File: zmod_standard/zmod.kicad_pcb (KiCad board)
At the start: 6 copper layers, 50 x 70 mm, 13 parts, among them J2 QTH-020-01-X-D-DP-A

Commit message: zmod_standard work
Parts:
- removed J2: QTH-020-01-X-D-DP-A, QTH:SAMTEC_QTH-020-01-X-D-DP-A
- removed R3: 100, Resistor_SMD:R_0603_1608Metric
- added J1: QTE-020-01-X-D-A, QTE:SAMTEC_QTE-020-01-X-D-A, F.Cu at (125.0, 57.0)
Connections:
- R1 pad 2: Net-(J2-Pad14) -> /led0
- R2 pad 2: Net-(J2-Pad16) -> /led1
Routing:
- net /hss1_N: track 353.6 -> 0.00 mm, vias 12 -> 0
- net /hss1_P: track 353.5 -> 0.00 mm, vias 12 -> 0
- net Net-(J2-Pad14): track 52.9 -> 0.00 mm, vias 2 -> 0
- net Net-(J2-Pad16): track 52.8 -> 0.00 mm, vias 2 -> 0
- net /led0: track 0.00 -> 49.9 mm
- net /led1: track 0.00 -> 49.7 mm, vias 0 -> 2
- net /lvdsclk_P: track 27.2 -> 0.00 mm
- net /lvdsclk_N: track 24.2 -> 0.00 mm
- net /lvds1_P: track 15.5 -> 0.00 mm, vias 2 -> 0
- net /lvds1_N: track 12.8 -> 0.00 mm, vias 2 -> 0
- net /lvds0_P: track 12.1 -> 0.00 mm, vias 2 -> 0
- net /d4_P: track 0.00 -> 11.8 mm, vias 0 -> 2
- net /d0_N: track 0.00 -> 11.3 mm, vias 0 -> 2
- net /d1_N: track 0.00 -> 11.3 mm, vias 0 -> 2
- net /lvds0_N: track 10.8 -> 0.00 mm, vias 2 -> 0
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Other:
- board text added: "ZMOD Standard Rev 1.0 WWW.HDLGUY.COM"
- board text removed: "ZMOD TXR-2 Rev 1.0 WWW.HDLGUY.COM"

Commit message: removed redundant fill planes on zmod boards
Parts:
- moved H2 5.00 mm to (140.0, 115.0)
- moved H5 5.00 mm to (139.5, 57.0)
- moved H6 5.00 mm to (140.0, 67.0)
- moved J1 2.50 mm to (122.5, 57.0)
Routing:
- net /led0: track 49.9 -> 0.00 mm
- net /led1: track 49.7 -> 0.00 mm, vias 2 -> 0
- net GND: track 14.9 -> 0.00 mm, vias 10 -> 0
- net /d4_P: track 11.8 -> 0.00 mm, vias 2 -> 0
- net /d0_N: track 11.3 -> 0.00 mm, vias 2 -> 0
- net /d1_N: track 11.3 -> 0.00 mm, vias 2 -> 0
- net /d4_N: track 10.7 -> 0.00 mm, vias 2 -> 0
- net /d0_P: track 10.4 -> 0.00 mm, vias 2 -> 0
- net /d1_P: track 9.39 -> 0.00 mm, vias 2 -> 0
- net /d5_P: track 9.13 -> 0.00 mm, vias 2 -> 0
- net /R_GA: track 8.76 -> 0.00 mm
- net /d5_N: track 8.40 -> 0.00 mm, vias 2 -> 0
- net /p2c_clk_N: track 7.01 -> 0.00 mm
- net /p2c_clk_P: track 7.01 -> 0.00 mm
- net /s24: track 4.44 -> 0.00 mm
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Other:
- board size 50 x 70 mm -> 45 x 70 mm

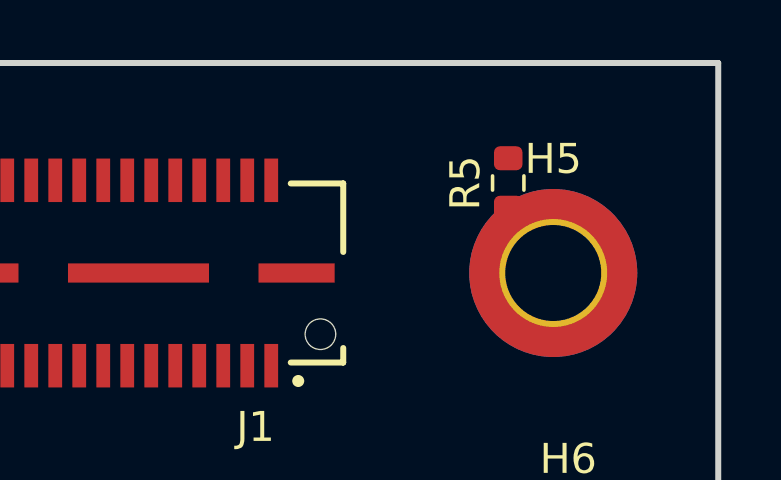
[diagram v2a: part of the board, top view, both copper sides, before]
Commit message: organizing local libraries, footprint and symbol
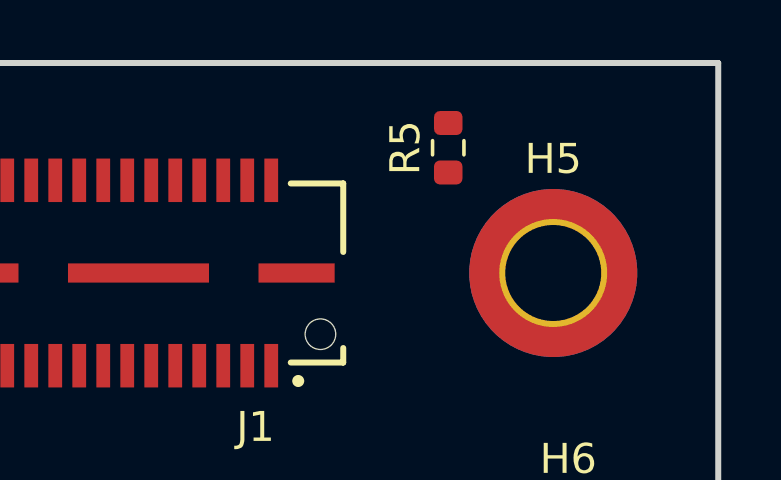
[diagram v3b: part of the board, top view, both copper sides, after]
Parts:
- J1: footprint QTE:SAMTEC_QTE-020-01-X-D-A -> pedrolib:SAMTEC_QTE-020-01-X-D-A
- moved R5 2.32 mm to (136.0, 52.8)
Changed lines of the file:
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@@
     (descr "LED SMD 0603 (1608 Metric), square (rectangular) end terminal, IPC_7351 nominal, (Body size source: http://www.tortai-tech.com/upload/download/2011102023233369053.pdf), generated with kicad-footprint-generator")
     (tags "LED")
-    (property "Sheetfile" "zmod.kicad_sch")
+    (property "Sheetfile" "File: zmod.kicad_sch")
     (property "Sheetname" "")
     (attr smd)
@@
     (descr "LED SMD 0603 (1608 Metric), square (rectangular) end terminal, IPC_7351 nominal, (Body size source: http://www.tortai-tech.com/upload/download/2011102023233369053.pdf), generated with kicad-footprint-generator")
     (tags "LED")
-    (property "Sheetfile" "zmod.kicad_sch")
+    (property "Sheetfile" "File: zmod.kicad_sch")
     (property "Sheetname" "")
     (attr smd)
@@
     (descr "Mounting Hole 3.2mm, M3, DIN965")
     (tags "mounting hole 3.2mm m3 din965")
-    (property "Sheetfile" "zmod.kicad_sch")
+    (property "Sheetfile" "File: zmod.kicad_sch")
     (property "Sheetname" "")
     (attr exclude_from_pos_files)
@@
     (descr "Resistor SMD 0603 (1608 Metric), square (rectangular) end terminal, IPC_7351 nominal, (Body size source: IPC-SM-782 page 72, https://www.pcb-3d.com/wordpress/wp-content/uploads/ipc-sm-782a_amendment_1_and_2.pdf), generated with kicad-footprint-generator")
     (tags "resistor")
-    (property "Sheetfile" "zmod.kicad_sch")
+    (property "Sheetfile" "File: zmod.kicad_sch")
     (property "Sheetname" "")
     (attr smd)
@@
     (descr "Mounting Hole 3.2mm, M3, DIN965")
     (tags "mounting hole 3.2mm m3 din965")
-    (property "Sheetfile" "zmod.kicad_sch")
+    (property "Sheetfile" "File: zmod.kicad_sch")
     (property "Sheetname" "")
     (attr exclude_from_pos_files)
@@
     (descr "Mounting Hole 3.2mm, M3, DIN965")
     (tags "mounting hole 3.2mm m3 din965")
-    (property "Sheetfile" "zmod.kicad_sch")
+    (property "Sheetfile" "File: zmod.kicad_sch")
     (property "Sheetname" "")
     (attr exclude_from_pos_files)
@@
     (descr "Mounting Hole 3.2mm, M3, DIN965")
     (tags "mounting hole 3.2mm m3 din965")
-    (property "Sheetfile" "zmod.kicad_sch")
+    (property "Sheetfile" "File: zmod.kicad_sch")
     (property "Sheetname" "")
     (attr exclude_from_pos_files)
@@
     (descr "Mounting Hole 3.2mm, M3, DIN965")
     (tags "mounting hole 3.2mm m3 din965")
-    (property "Sheetfile" "zmod.kicad_sch")
+    (property "Sheetfile" "File: zmod.kicad_sch")
     (property "Sheetname" "")
     (attr exclude_from_pos_files)
@@
       (net 9 "unconnected-(H4-Pad1)") (pinfunction "1") (pintype "input"))
   )
-  (footprint "QTE:SAMTEC_QTE-020-01-X-D-A" locked (layer "F.Cu")
+  (footprint "pedrolib:SAMTEC_QTE-020-01-X-D-A" locked (layer "F.Cu")
     (at 122.5 57 180)
     (property "MANUFACTURER" "Samtec")
@@
     (property "PARTREV" "K")
     (property "STANDARD" "Manufacturer Recommendations")
-    (property "Sheetfile" "zmod.kicad_sch")
+    (property "Sheetfile" "File: zmod.kicad_sch")
     (property "Sheetname" "")
     (attr through_hole)
@@
       (effects (font (size 1 1) (thickness 0.15)))
     )
-    (fp_line (start -8.25 -2.9845) (end -10 -2.9845) (layer "F.SilkS") (width 0.2))
-    (fp_line (start 8.25 -2.9845) (end 10 -2.9845) (layer "F.SilkS") (width 0.2))
-    (fp_line (start 10 -2.9845) (end 10 -2.5) (layer "F.SilkS") (width 0.2))
-    (fp_line (start -10 0.7) (end -10 2.9845) (layer "F.SilkS") (width 0.2))
     (fp_line (start 8.25 2.9845) (end 10 2.9845) (layer "F.SilkS") (width 0.2))
     (fp_line (start -10 2.9845) (end -8.25 2.9845) (layer "F.SilkS") (width 0.2))
     (fp_line (start -10 -2.9845) (end -10 -2.5) (layer "F.SilkS") (width 0.2))
+    (fp_line (start -10 0.7) (end -10 2.9845) (layer "F.SilkS") (width 0.2))
     (fp_line (start 10 2.9845) (end 10 0.7) (layer "F.SilkS") (width 0.2))
+    (fp_line (start -8.25 -2.9845) (end -10 -2.9845) (layer "F.SilkS") (width 0.2))
+    (fp_line (start 10 -2.9845) (end 10 -2.5) (layer "F.SilkS") (width 0.2))
+    (fp_line (start 8.25 -2.9845) (end 10 -2.9845) (layer "F.SilkS") (width 0.2))
     (fp_circle (center -8.5 -3.6) (end -8.4 -3.6) (layer "F.SilkS") (width 0.2) (fill none))
+    (fp_line (start -10.25 4.065) (end 10.25 4.065) (layer "F.CrtYd") (width 0.05))
     (fp_line (start 10.25 4.065) (end 10.25 -4.065) (layer "F.CrtYd") (width 0.05))
+    (fp_line (start 10.25 -4.065) (end -10.25 -4.065) (layer "F.CrtYd") (width 0.05))
     (fp_line (start -10.25 -4.065) (end -10.25 4.065) (layer "F.CrtYd") (width 0.05))
-    (fp_line (start -10.25 4.065) (end 10.25 4.065) (layer "F.CrtYd") (width 0.05))
-    (fp_line (start 10.25 -4.065) (end -10.25 -4.065) (layer "F.CrtYd") (width 0.05))
+    (fp_line (start -10 -2.9845) (end 10 -2.9845) (layer "F.Fab") (width 0.1))
+    (fp_line (start -10 2.9845) (end -10 -2.9845) (layer "F.Fab") (width 0.1))
+    (fp_line (start 10 -2.9845) (end 10 2.9845) (layer "F.Fab") (width 0.1))
     (fp_line (start 10 2.9845) (end -10 2.9845) (layer "F.Fab") (width 0.1))
-    (fp_line (start -10 2.9845) (end -10 -2.9845) (layer "F.Fab") (width 0.1))
-    (fp_line (start -10 -2.9845) (end 10 -2.9845) (layer "F.Fab") (width 0.1))
-    (fp_line (start 10 -2.9845) (end 10 2.9845) (layer "F.Fab") (width 0.1))
     (fp_circle (center -8.5 -3.6) (end -8.4 -3.6) (layer "F.Fab") (width 0.2) (fill none))
     (pad "" np_thru_hole circle locked (at 9.24 -2.04 180) (size 1.02 1.02) (drill 1.02) (layers *.Cu *.Mask))
@@
     (descr "Resistor SMD 0603 (1608 Metric), square (rectangular) end terminal, IPC_7351 nominal, (Body size source: IPC-SM-782 page 72, https://www.pcb-3d.com/wordpress/wp-content/uploads/ipc-sm-782a_amendment_1_and_2.pdf), generated with kicad-footprint-generator")
     (tags "resistor")
-    (property "Sheetfile" "zmod.kicad_sch")
+    (property "Sheetfile" "File: zmod.kicad_sch")
     (property "Sheetname" "")
     (attr smd)
@@
     (descr "Mounting Hole 3.2mm, M3, DIN965")
     (tags "mounting hole 3.2mm m3 din965")
-    (property "Sheetfile" "zmod.kicad_sch")
+    (property "Sheetfile" "File: zmod.kicad_sch")
     (property "Sheetname" "")
     (attr exclude_from_pos_files)
@@
   )
   (footprint "Resistor_SMD:R_0603_1608Metric" (layer "F.Cu")
-    (at 138 54 90)
+    (at 136 52.825 90)
     (descr "Resistor SMD 0603 (1608 Metric), square (rectangular) end terminal, IPC_7351 nominal, (Body size source: IPC-SM-782 page 72, https://www.pcb-3d.com/wordpress/wp-content/uploads/ipc-sm-782a_amendment_1_and_2.pdf), generated with kicad-footprint-generator")
     (tags "resistor")
-    (property "Sheetfile" "zmod.kicad_sch")
+    (property "Sheetfile" "File: zmod.kicad_sch")
     (property "Sheetname" "")
     (attr smd)
